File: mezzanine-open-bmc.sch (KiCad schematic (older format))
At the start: 2 parts, among them P1 CONN_02X20, P2 CONN_02X20

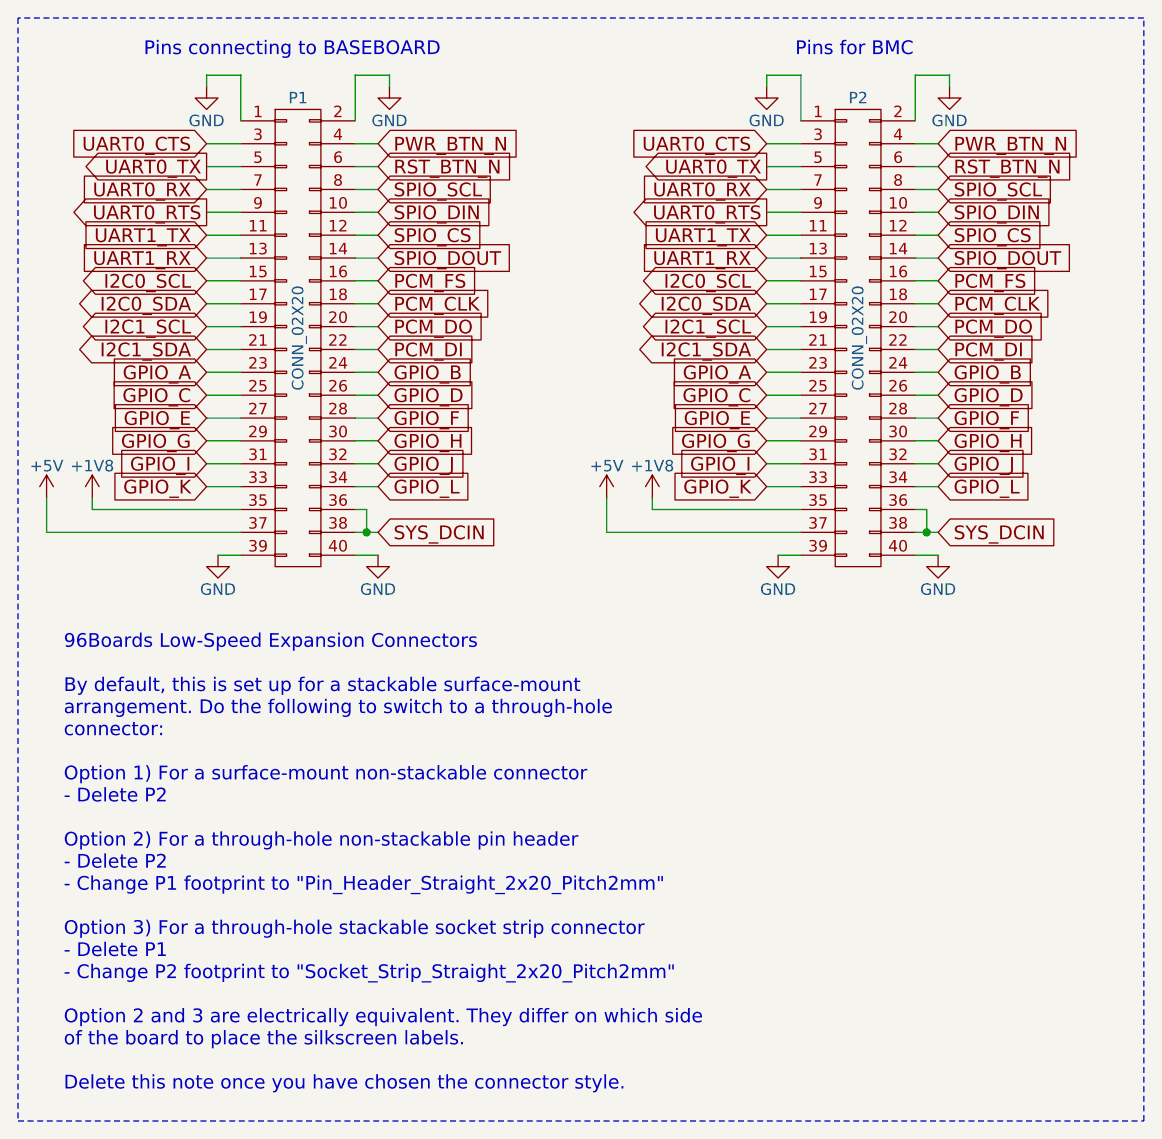
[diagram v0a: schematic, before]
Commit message: Add PWR & RST Switches for BMC
Buttons/Switches are now connected to the top-side pins for
Power and Reset.

Signed-off-by: Sophie Haynes <sophie.haynes@linaro.org>
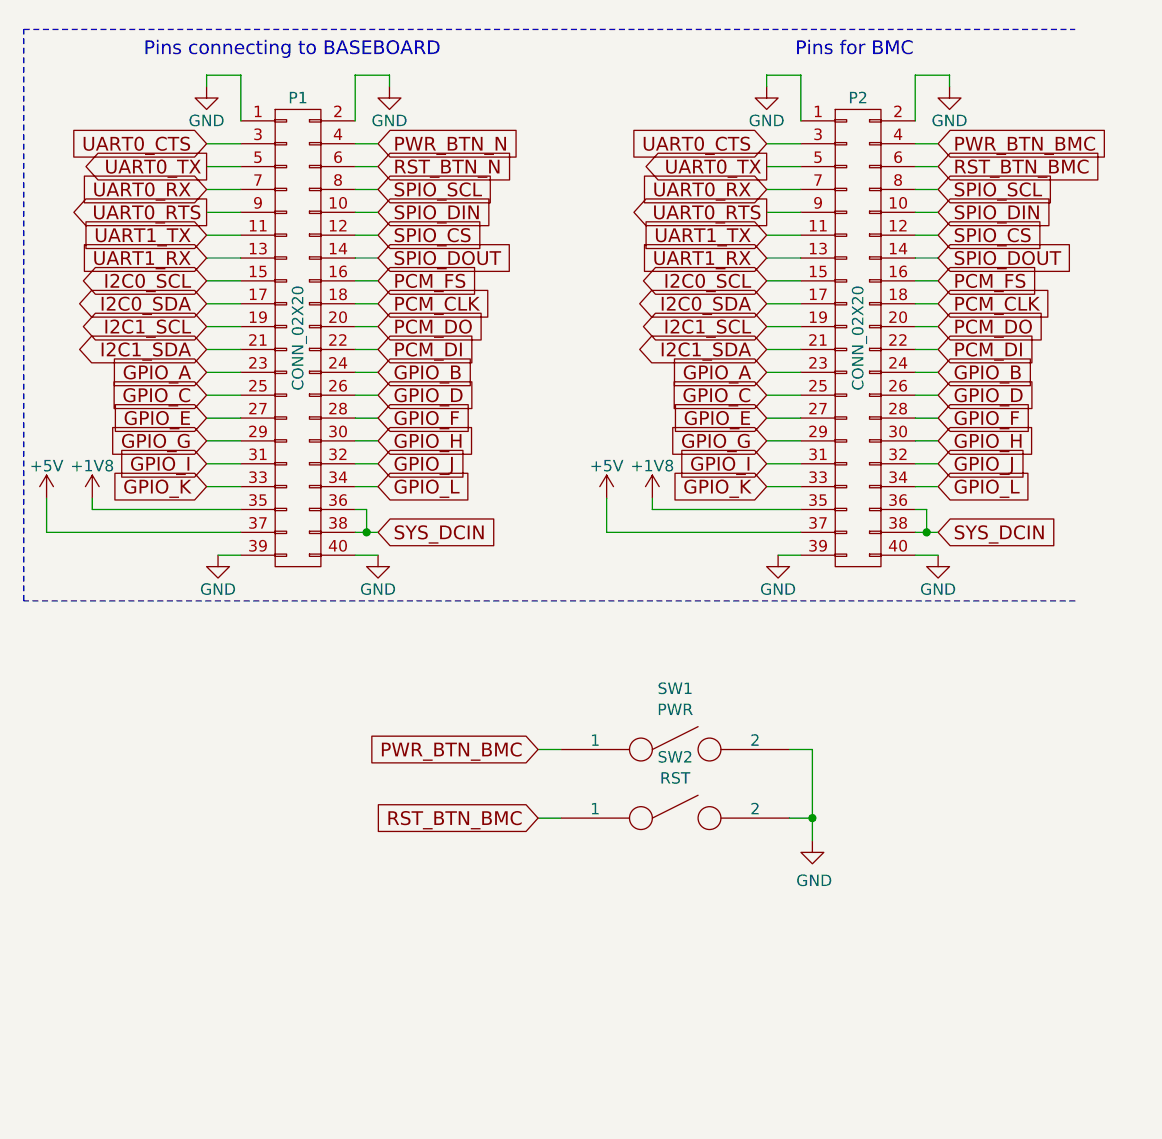
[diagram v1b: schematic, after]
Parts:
- added SW1: PWR, symbol SPST
- added SW2: RST, symbol SPST
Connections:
- net GND: now also SW1.2, SW2.2
- net PWR_BTN_N: no longer P2.4 (P4)
- net RST_BTN_N: no longer P2.6 (P6)
- new net PWR_BTN_BMC: P2.4 (P4), SW1.1
- new net RST_BTN_BMC: P2.6 (P6), SW2.1
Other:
- note removed: "96Boards Low-Speed Expansion Connectors\n\nBy default, this is set up for a stackable surface-mount\narrangement. Do the following to switch to a through-hole\nconnector:\n\nOption 1) For a surface-mount non-stackable connector\n- Delete P2\n\nOption 2) For a through-hole non-stackable pin header\n- Delete P2\n- Change P1 footprint to "Pin_Header_Straight_2x20_Pitch2mm"\n\nOption 3) For a through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"
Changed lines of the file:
@@
 UART0_RTS
 $Comp
-L GND #PWR01
+L GND #PWR9
 U 1 1 55D481C7
 P 3950 950
-F 0 "#PWR01" H 3950 700 50  0001 C CNN
+F 0 "#PWR9" H 3950 700 50  0001 C CNN
 F 1 "GND" H 3950 800 50  0000 C CNN
 F 2 "" H 3950 950 60  0000 C CNN
@@
 UART0_TX
 $Comp
-L GND #PWR02
+L GND #PWR10
 U 1 1 55D481CF
 P 4000 3000
-F 0 "#PWR02" H 4000 2750 50  0001 C CNN
+F 0 "#PWR10" H 4000 2750 50  0001 C CNN
 F 1 "GND" H 4000 2850 50  0000 C CNN
 F 2 "" H 4000 3000 60  0000 C CNN
@@
 $EndComp
 $Comp
-L GND #PWR03
+L GND #PWR12
 U 1 1 55D481D5
 P 4700 3000
-F 0 "#PWR03" H 4700 2750 50  0001 C CNN
+F 0 "#PWR12" H 4700 2750 50  0001 C CNN
 F 1 "GND" H 4700 2850 50  0000 C CNN
 F 2 "" H 4700 3000 60  0000 C CNN
@@
 SYS_DCIN
 $Comp
-L GND #PWR04
+L GND #PWR13
 U 1 1 55D48218
 P 4750 950
-F 0 "#PWR04" H 4750 700 50  0001 C CNN
+F 0 "#PWR13" H 4750 700 50  0001 C CNN
 F 1 "GND" H 4750 800 50  0000 C CNN
 F 2 "" H 4750 950 60  0000 C CNN
@@
 $EndComp
 $Comp
-L +1V8 #PWR05
+L +1V8 #PWR8
 U 1 1 55D4822C
 P 3450 2750
-F 0 "#PWR05" H 3450 2600 50  0001 C CNN
+F 0 "#PWR8" H 3450 2600 50  0001 C CNN
 F 1 "+1V8" H 3450 2890 50  0000 C CNN
 F 2 "" H 3450 2750 60  0000 C CNN
@@
 $EndComp
 $Comp
-L +5V #PWR06
+L +5V #PWR7
 U 1 1 55D48233
 P 3250 2750
-F 0 "#PWR06" H 3250 2600 50  0001 C CNN
+F 0 "#PWR7" H 3250 2600 50  0001 C CNN
 F 1 "+5V" H 3250 2890 50  0000 C CNN
 F 2 "" H 3250 2750 60  0000 C CNN
@@
 $EndComp
 Text GLabel 4700 1300 2    60   Input ~ 0
-RST_BTN_N
+RST_BTN_BMC
 Text GLabel 3950 2100 0    60   BiDi ~ 0
 I2C1_SDA
@@
 Text GLabel 3950 1400 0    60   Input ~ 0
 UART0_RX
-Text Notes 875  5350 0    60   ~ 0
-96Boards Low-Speed Expansion Connectors\n\nBy default, this is set up for a stackable surface-mount\narrangement. Do the following to switch to a through-hole\nconnector:\n\nOption 1) For a surface-mount non-stackable connector\n- Delete P2\n\nOption 2) For a through-hole non-stackable pin header\n- Delete P2\n- Change P1 footprint to "Pin_Header_Straight_2x20_Pitch2mm"\n\nOption 3) For a through-hole stackable socket strip connector\n- Delete P1\n- Change P2 footprint to "Socket_Strip_Straight_2x20_Pitch2mm"\n\nOption 2 and 3 are electrically equivalent. They differ on which side\nof the board to place the silkscreen labels.\n\nDelete this note once you have chosen the connector style.
 Text GLabel 4700 1200 2    60   Input ~ 0
-PWR_BTN_N
+PWR_BTN_BMC
 Text GLabel 3950 1600 0    60   Input ~ 0
 UART1_TX
@@
 	4100 1500 3950 1500
 $Comp
-L GND #PWR07
+L GND #PWR3
 U 1 1 55BEAA68
 P 1500 950
-F 0 "#PWR07" H 1500 700 50  0001 C CNN
+F 0 "#PWR3" H 1500 700 50  0001 C CNN
 F 1 "GND" H 1500 800 50  0000 C CNN
 F 2 "" H 1500 950 60  0000 C CNN
@@
 $EndComp
 $Comp
-L GND #PWR08
+L GND #PWR4
 U 1 1 55BEA10A
 P 1550 3000
-F 0 "#PWR08" H 1550 2750 50  0001 C CNN
+F 0 "#PWR4" H 1550 2750 50  0001 C CNN
 F 1 "GND" H 1550 2850 50  0000 C CNN
 F 2 "" H 1550 3000 60  0000 C CNN
@@
 $EndComp
 $Comp
-L GND #PWR09
+L GND #PWR5
 U 1 1 55BEA0BC
 P 2250 3000
-F 0 "#PWR09" H 2250 2750 50  0001 C CNN
+F 0 "#PWR5" H 2250 2750 50  0001 C CNN
 F 1 "GND" H 2250 2850 50  0000 C CNN
 F 2 "" H 2250 3000 60  0000 C CNN
@@
 SYS_DCIN
 $Comp
-L GND #PWR010
+L GND #PWR6
 U 1 1 55D43BD4
 P 2300 950
-F 0 "#PWR010" H 2300 700 50  0001 C CNN
+F 0 "#PWR6" H 2300 700 50  0001 C CNN
 F 1 "GND" H 2300 800 50  0000 C CNN
 F 2 "" H 2300 950 60  0000 C CNN
@@
 $EndComp
 $Comp
-L +1V8 #PWR011
+L +1V8 #PWR2
 U 1 1 55D43CFB
 P 1000 2750
-F 0 "#PWR011" H 1000 2600 50  0001 C CNN
+F 0 "#PWR2" H 1000 2600 50  0001 C CNN
 F 1 "+1V8" H 1000 2890 50  0000 C CNN
 F 2 "" H 1000 2750 60  0000 C CNN
@@
 $EndComp
 $Comp
-L +5V #PWR012
+L +5V #PWR1
 U 1 1 55D440FD
 P 800 2750
-F 0 "#PWR012" H 800 2600 50  0001 C CNN
+F 0 "#PWR1" H 800 2600 50  0001 C CNN
 F 1 "+5V" H 800 2890 50  0000 C CNN
 F 2 "" H 800 2750 60  0000 C CNN
@@
 Pins for BMC
 Wire Notes Line
-	675  650  675  5475
+	5300 3200 700  3200
 Wire Notes Line
-	675  5475 5600 5475
+	700  3200 700  700
 Wire Notes Line
-	5600 5475 5600 650
-Wire Notes Line
-	5600 650  675  650
+	700  700  5300 700
+Text GLabel 2950 4150 0    60   Input ~ 0
+RST_BTN_BMC
+Text GLabel 2950 3850 0    60   Input ~ 0
+PWR_BTN_BMC
+$Comp
+L SPST SW1
+U 1 1 56D59D87
+P 3550 3850
+F 0 "SW1" H 3550 4116 50  0000 C CNN
+F 1 "PWR" H 3550 4024 50  0000 C CNN
+F 2 "" H 3550 3850 50  0000 C CNN
+F 3 "" H 3550 3850 50  0000 C CNN
+	1    3550 3850
+	1    0    0    -1
+$EndComp
+$Comp
+L SPST SW2
+U 1 1 56D59DC4
+P 3550 4150
+F 0 "SW2" H 3550 4416 50  0000 C CNN
+F 1 "RST" H 3550 4324 50  0000 C CNN
+F 2 "" H 3550 4150 50  0000 C CNN
+F 3 "" H 3550 4150 50  0000 C CNN
+	1    3550 4150
+	1    0    0    -1
+$EndComp
+Wire Wire Line
+	2950 3850 3050 3850
+Wire Wire Line
+	2950 4150 3050 4150
+$Comp
+L GND #PWR11
+U 1 1 56D59F1C
+P 4150 4250
+F 0 "#PWR11" H 4150 4000 50  0001 C CNN
+F 1 "GND" H 4158 4076 50  0000 C CNN
+F 2 "" H 4150 4250 50  0000 C CNN
+F 3 "" H 4150 4250 50  0000 C CNN
+	1    4150 4250
+	1    0    0    -1
+$EndComp
+Wire Wire Line
+	4150 4250 4150 3850
+Wire Wire Line
+	4150 3850 4050 3850
+Wire Wire Line
+	4050 4150 4150 4150
+Connection ~ 4150 4150
 $EndSCHEMATC
